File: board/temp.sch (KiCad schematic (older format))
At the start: 3 parts

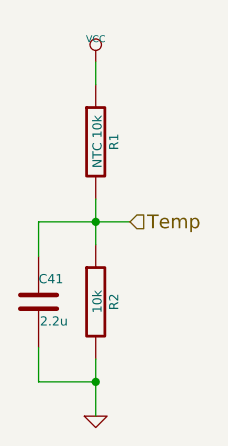
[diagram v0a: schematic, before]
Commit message: - implemented complementary transistor package - started layout
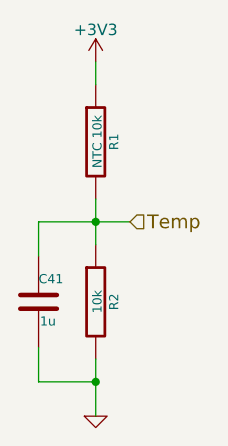
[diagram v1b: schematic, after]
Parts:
- C41: value 2.2u -> 1u; footprint CRF1:SMD-0603_c -> Capacitors_SMD:C_0805
- R1: footprint CRF1:SMD-0603_r -> Resistors_SMD:R_0603
- R2: footprint CRF1:SMD-0603_r -> Resistors_SMD:R_0805
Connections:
- net VCC renamed +3V3
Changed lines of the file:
@@
 F 0 "R1" V 4480 3400 40  0000 C CNN
 F 1 "NTC 10k" V 4407 3401 40  0000 C CNN
-F 2 "CRF1:SMD-0603_r" V 4330 3400 30  0001 C CNN
+F 2 "Resistors_SMD:R_0603" V 4330 3400 30  0001 C CNN
 F 3 "" H 4400 3400 30  0000 C CNN
 	1    4400 3400
@@
 F 0 "R2" V 4480 4100 40  0000 C CNN
 F 1 "10k" V 4407 4101 40  0000 C CNN
-F 2 "CRF1:SMD-0603_r" V 4330 4100 30  0001 C CNN
+F 2 "Resistors_SMD:R_0805" V 4330 4100 30  0001 C CNN
 F 3 "" H 4400 4100 30  0000 C CNN
 	1    4400 4100
@@
 P 4150 4100
 F 0 "C41" H 4150 4200 40  0000 L CNN
-F 1 "2.2u" H 4156 4015 40  0000 L CNN
-F 2 "CRF1:SMD-0603_c" H 4188 3950 30  0001 C CNN
+F 1 "1u" H 4156 4015 40  0000 L CNN
+F 2 "Capacitors_SMD:C_0805" H 4188 3950 30  0001 C CNN
 F 3 "" H 4150 4100 60  0000 C CNN
 	1    4150 4100
@@
 $EndComp
 $Comp
-L VCC #PWR023
-U 1 1 5426DB11
-P 4400 3050
-F 0 "#PWR023" H 4400 3150 30  0001 C CNN
-F 1 "VCC" H 4400 3150 30  0000 C CNN
-F 2 "" H 4400 3050 60  0000 C CNN
-F 3 "" H 4400 3050 60  0000 C CNN
-	1    4400 3050
-	1    0    0    -1
-$EndComp
-$Comp
-L GND-RESCUE-BLDC_4 #PWR024
+L GND-RESCUE-BLDC_4 #PWR041
 U 1 1 5426DB25
 P 4400 4600
-F 0 "#PWR024" H 4400 4600 30  0001 C CNN
+F 0 "#PWR041" H 4400 4600 30  0001 C CNN
 F 1 "GND" H 4400 4530 30  0001 C CNN
 F 2 "" H 4400 4600 60  0000 C CNN
@@
 Text HLabel 4550 3750 2    60   Input ~ 0
 Temp
+$Comp
+L +3V3 #PWR?
+U 1 1 57646387
+P 4400 3050
+F 0 "#PWR?" H 4400 2900 50  0001 C CNN
+F 1 "+3V3" H 4400 3190 50  0000 C CNN
+F 2 "" H 4400 3050 60  0000 C CNN
+F 3 "" H 4400 3050 60  0000 C CNN
+	1    4400 3050
+	1    0    0    -1
+$EndComp
 $EndSCHEMATC
